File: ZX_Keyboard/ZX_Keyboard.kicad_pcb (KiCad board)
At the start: 2 copper layers, 101.6 x 50.8 mm, 135 parts, among them J1 DBG_UART, J2 BOOT2, J3 SWD, J4 BOOT, SW1 RESET, U1 STM32F105R8Tx, Y1 8MHz

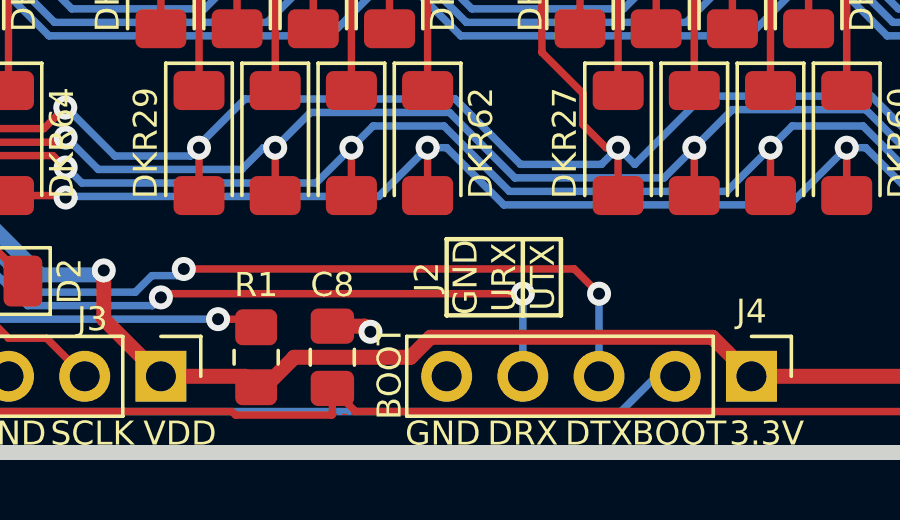
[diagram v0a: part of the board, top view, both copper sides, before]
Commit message: update model for ZX-Spectrum-Keyboard & ZX_Keyboard
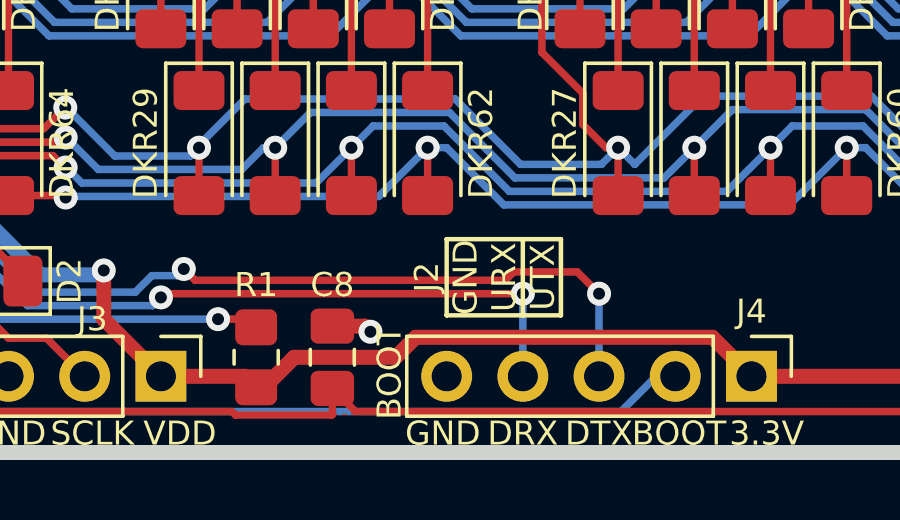
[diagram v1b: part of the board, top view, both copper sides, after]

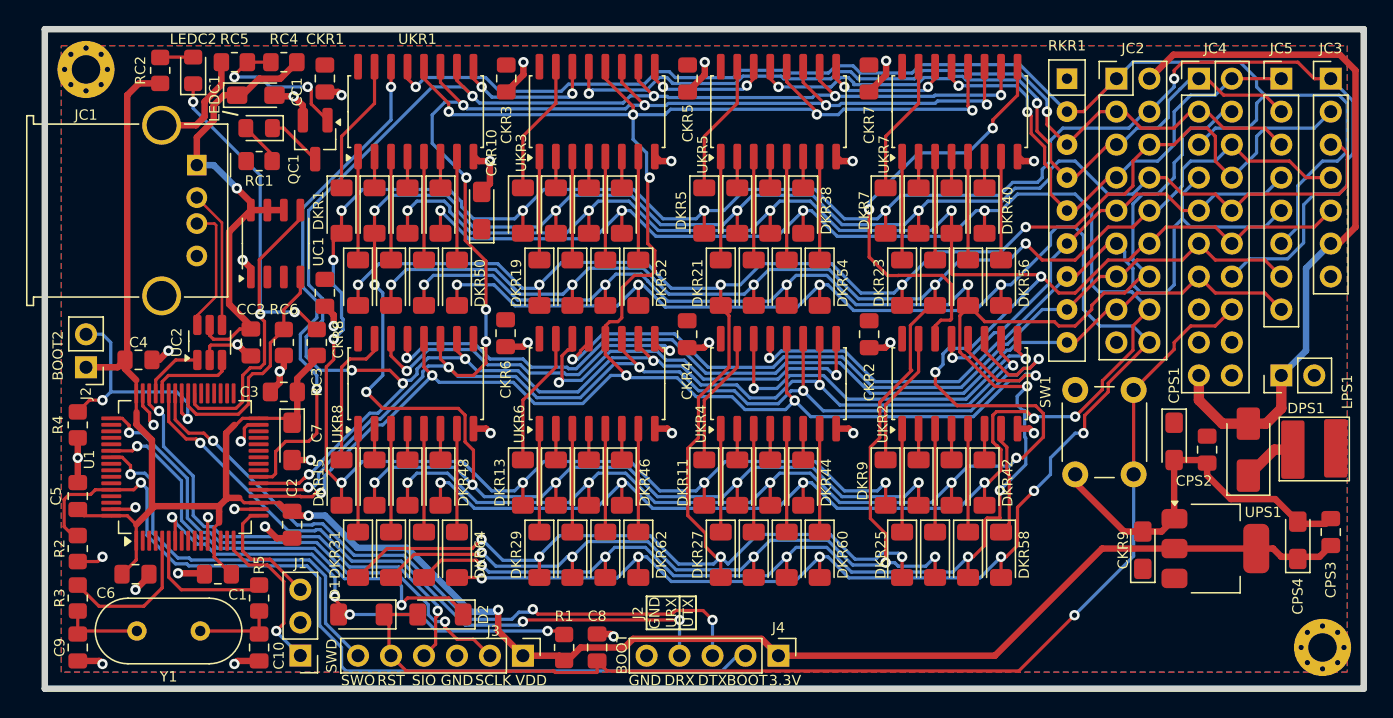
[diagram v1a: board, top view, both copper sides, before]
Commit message: delete R3 R5 repracing
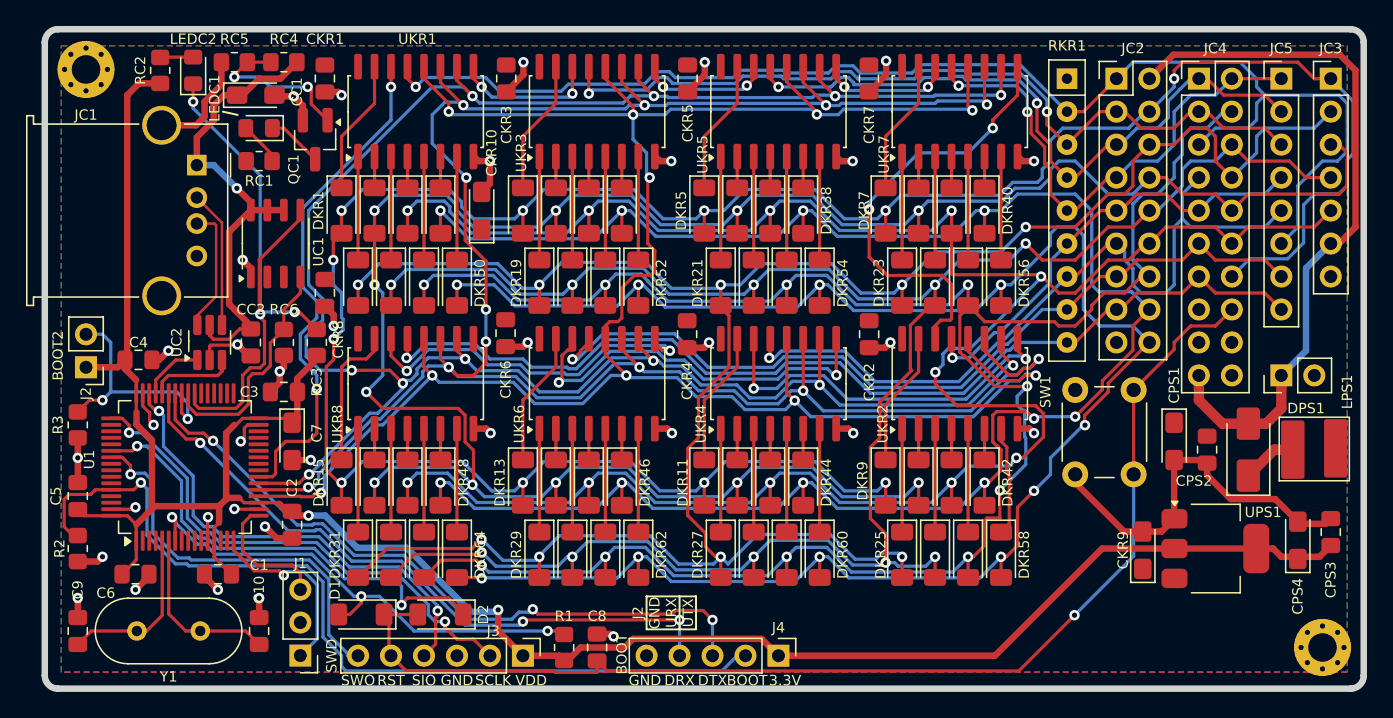
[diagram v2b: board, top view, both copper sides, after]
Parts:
- removed the R3 at (27.9, 69.2)
- removed R5: 0Om, Resistor_SMD:R_0805_2012Metric_Pad1.20x1.40mm_HandSolder
- moved C10 1.27 mm to (41.9, 71.8), turned to 90 degrees
- moved C9 1.27 mm to (27.9, 71.8), turned to 90 degrees
- renumbered R4 to R3
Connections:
- C10 pad 1: Net-(C10-Pad1) -> OSC_OUT
- C9 pad 1: Net-(C9-Pad1) -> OSC_IN
- Y1 pad 1: Net-(C10-Pad1) -> OSC_OUT
- Y1 pad 2: Net-(C9-Pad1) -> OSC_IN
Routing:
- net Net-(C9-Pad1): track 6.42 -> 0.00 mm
- net Net-(C10-Pad1): track 6.40 -> 0.00 mm
- net OSC_OUT: track 10.3 -> 13.6 mm
- net UTX: track 12.3 -> 14.5 mm
- net OSC_IN: track 11.4 -> 13.2 mm
- net GND: track 112.7 -> 111.3 mm
- net Net-(D1-A): track 37.0 -> 38.1 mm, vias 4 -> 3
- net URX: track 9.25 -> 9.99 mm
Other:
- outline, holes or cut-outs redrawn

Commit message: update keyboard connection
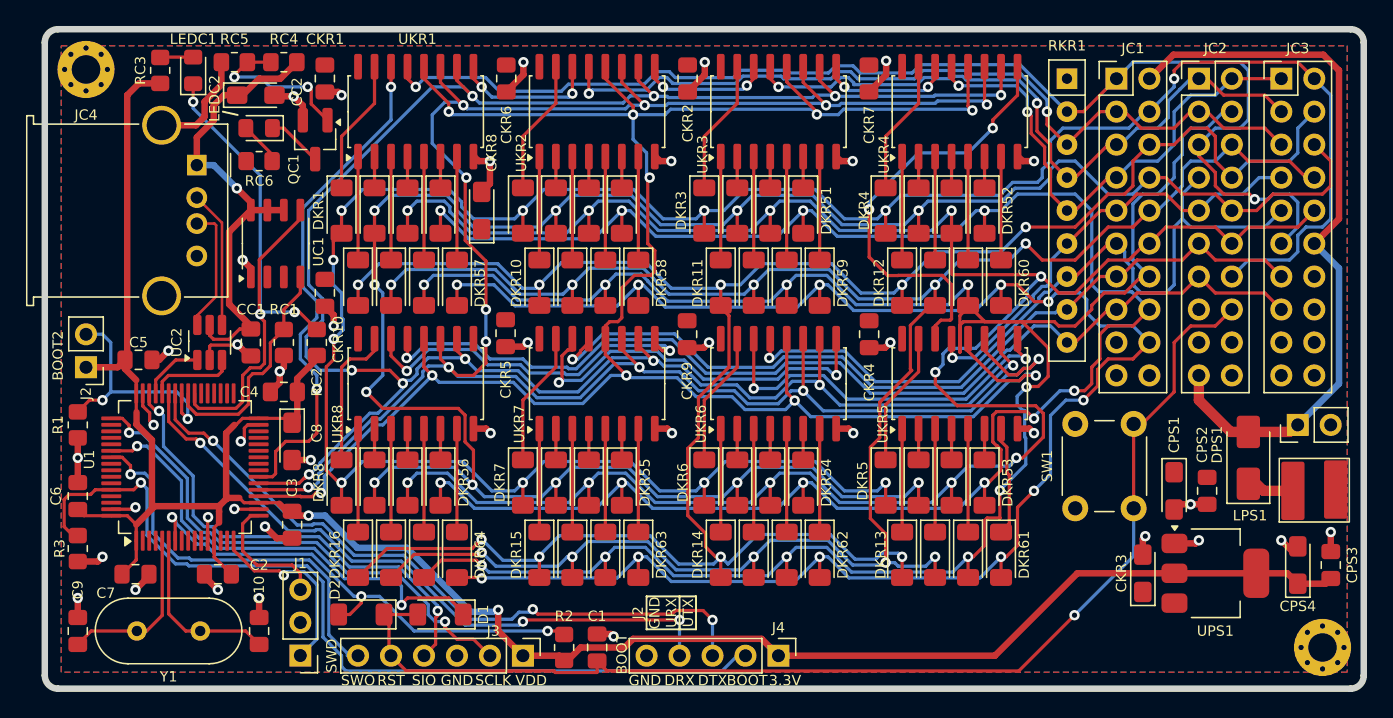
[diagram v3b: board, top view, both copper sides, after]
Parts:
- removed JC5: ZX_Address, Connector_PinHeader_2.54mm:PinHeader_1x08_P2.54mm_Vertical
- JC1: renamed from JC2; footprint Connector_PinHeader_2.54mm:PinHeader_2x09_P2.54mm_Vertical -> Connector_PinHeader_2.54mm:PinHeader_2x10_P2.54mm_Vertical
- JC3: value ZX_Date -> ZX_Keyboard; footprint Connector_PinHeader_2.54mm:PinHeader_1x07_P2.54mm_Vertical -> Connector_PinHeader_2.54mm:PinHeader_2x10_P2.54mm_Vertical
- moved JPS1 4.01 mm to (121.9, 55.9)
- moved CPS1 3.81 mm to (112.4, 61.0)
- moved JC3 3.81 mm to (120.7, 29.2)
- moved CPS2 3.18 mm to (114.9, 61.0)
- moved LPS1 3.18 mm to (123.2, 61.0)
- moved SW1 2.62 mm to (104.8, 62.3)
- moved CPS3 2.54 mm to (124.5, 66.7)
- moved CPS4 1.91 mm to (121.9, 66.7)
- moved UPS1 1.91 mm to (115.6, 67.3)
- moved CKR3 1.78 mm to (110.0, 67.3)
- moved DPS1 0.64 mm to (118.1, 58.4)
- renumbered C8 to C1, C1 to C2, C2 to C3, C3 to C4, C4 to C5, C5 to C6, C6 to C7, C7 to C8, CC2 to CC1, CC1 to CC2, CKR8 to CKR10, CKR5 to CKR2, CKR9 to CKR3, CKR2 to CKR4, CKR6 to CKR5, CKR3 to CKR6, CKR10 to CKR8, CKR4 to CKR9, D2 to D1, D1 to D2, DKR19 to DKR10, DKR21 to DKR11, DKR23 to DKR12, DKR25 to DKR13, DKR27 to DKR14, DKR29 to DKR15, DKR31 to DKR16, DKR33 to DKR17, DKR35 to DKR18, DKR37 to DKR19, DKR3 to DKR2, DKR39 to DKR20, DKR41 to DKR21, DKR43 to DKR22, DKR45 to DKR23, DKR47 to DKR24, DKR49 to DKR25, DKR51 to DKR26, DKR53 to DKR27, DKR55 to DKR28, DKR57 to DKR29, DKR5 to DKR3, DKR59 to DKR30, DKR61 to DKR31, DKR63 to DKR32, DKR2 to DKR33, DKR4 to DKR34, DKR6 to DKR35, DKR8 to DKR36, DKR10 to DKR37, DKR12 to DKR38, DKR14 to DKR39, DKR7 to DKR4, DKR16 to DKR40, DKR18 to DKR41, DKR20 to DKR42, DKR22 to DKR43, DKR24 to DKR44, DKR26 to DKR45, DKR28 to DKR46, DKR30 to DKR47, DKR32 to DKR48, DKR34 to DKR49, DKR9 to DKR5, DKR36 to DKR50, DKR38 to DKR51, DKR40 to DKR52, DKR42 to DKR53, DKR44 to DKR54, DKR46 to DKR55, DKR48 to DKR56, DKR50 to DKR57, DKR52 to DKR58, DKR54 to DKR59, DKR11 to DKR6, DKR56 to DKR60, DKR58 to DKR61, DKR60 to DKR62, DKR62 to DKR63, DKR13 to DKR7, DKR15 to DKR8, DKR17 to DKR9, JC4 to JC2, JC1 to JC4, LEDC2 to LEDC1, LEDC1 to LEDC2, R3 to R1, R1 to R2, R2 to R3, RC6 to RC1, RC3 to RC2, RC2 to RC3, RC1 to RC6, UKR3 to UKR2, UKR5 to UKR3, UKR7 to UKR4, UKR2 to UKR5, UKR4 to UKR6, UKR6 to UKR7
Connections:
- JC2 pad 18: unconnected-(JC4-Pin_18-Pad18) -> GND
- JC2 pad 20: unconnected-(JC4-Pin_20-Pad20) -> GND
- JC3 pad 1: KeyD0 -> KeyA11
- JC3 pad 2: KeyD1 -> KeyD0
- JC3 pad 3: KeyD2 -> KeyA10
- JC3 pad 4: KeyD3 -> KeyD1
- JC3 pad 5: KeyD4 -> KeyA9
- JC3 pad 6: VIN+5V -> KeyD2
- JC3 pad 7: GND -> KeyA12
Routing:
- net GND: track 111.3 -> 90.6 mm, vias 35 -> 40
- net KeyD5: track 166.2 -> 174.0 mm
- net KeyA8: track 101.9 -> 94.9 mm, vias 1 -> 2
- net KeyD7: track 146.1 -> 141.5 mm, vias 10 -> 11
- net KeyD0: track 194.3 -> 191.9 mm
- net KeyD2: track 178.8 -> 177.1 mm
- net VIN+5V: track 55.4 -> 56.9 mm
- net KeyD3: track 166.1 -> 164.9 mm
- net KeyA15: track 78.2 -> 79.3 mm
- net +3.3V: track 176.5 -> 175.4 mm
- net KeyD4: track 178.6 -> 177.6 mm
- net KeyD1: track 173.4 -> 172.5 mm
- net ~{RST}: track 92.4 -> 91.8 mm

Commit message: update pcb
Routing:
- net KeyD5: track 174.0 -> 165.6 mm
- net KeyD4: track 177.6 -> 169.4 mm
- net SCK: track 168.8 -> 167.4 mm
- net KeyD6: track 152.0 -> 151.2 mm, vias 10 -> 9
- net Net-(UKR4-SOUT): track 34.0 -> 33.5 mm

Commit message: add label
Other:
- board text added: "USB ZX keyboard Version V1.00 alexsyrezerv@mail.ru"
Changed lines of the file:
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@@
 		(layer "Edge.Cuts")
+	)
+	(gr_text "USB ZX keyboard\nVersion V1.00\nalexsyrezerv@mail.ru\n"
+		(at 72.136 49.276 0)
+		(layer "B.SilkS")
+		(effects
+			(font
+				(size 3 3)
+				(thickness 0.6)
+				(bold yes)
+			)
+			(justify mirror)
+		)
 	)
 	(gr_text "SWO"

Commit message: update Schematic and PCB
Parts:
- C8, CKR3, CKR8: value 4.7uFx6.3V -> 4,7uFx6,3V
- CC2: value 4,7uFx6.3V -> 4,7uFx6,3V
- CPS1, CPS4: value 10uFx6.3v -> 10uFx6,3v
